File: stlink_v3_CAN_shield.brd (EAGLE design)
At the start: 64.8 x 40.6 mm, 13 parts, among them CON1 STLINK_V3, U1 MCP2562-E/SN

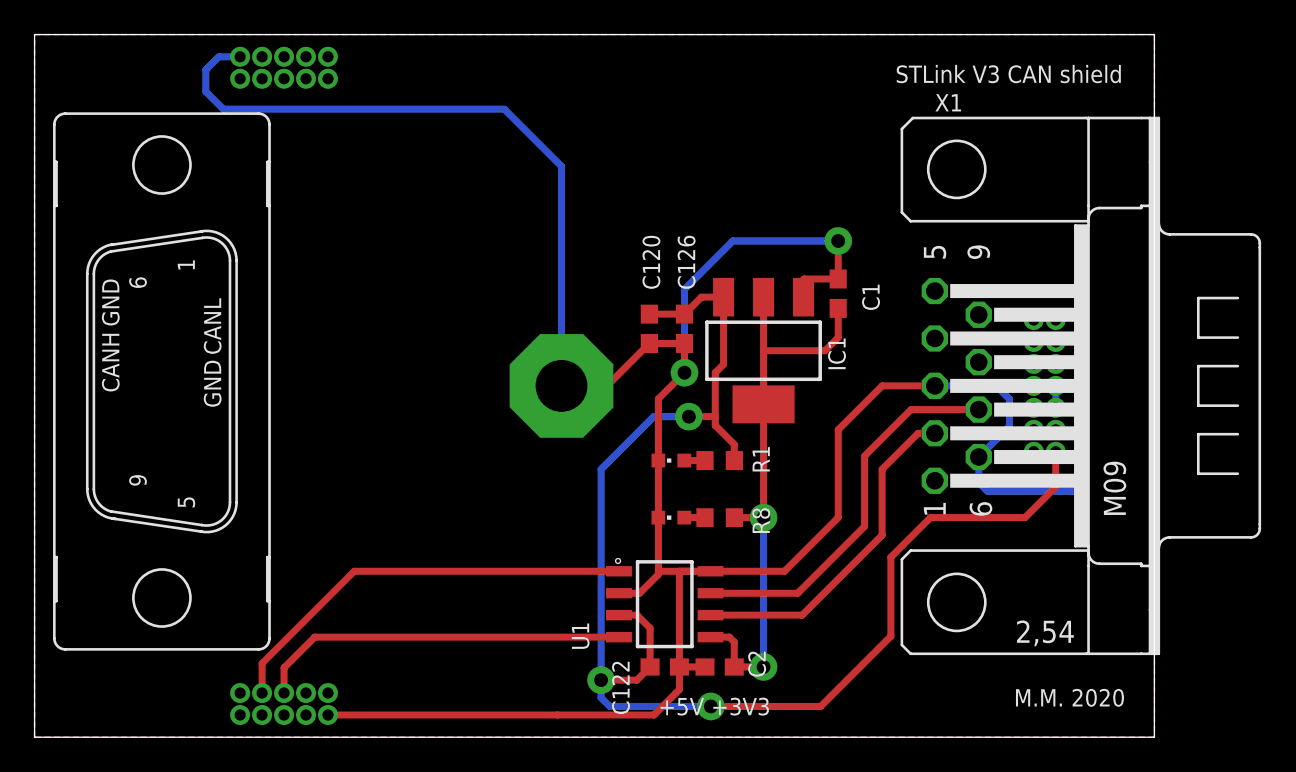
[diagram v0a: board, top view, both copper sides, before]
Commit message: Update STLink footprint
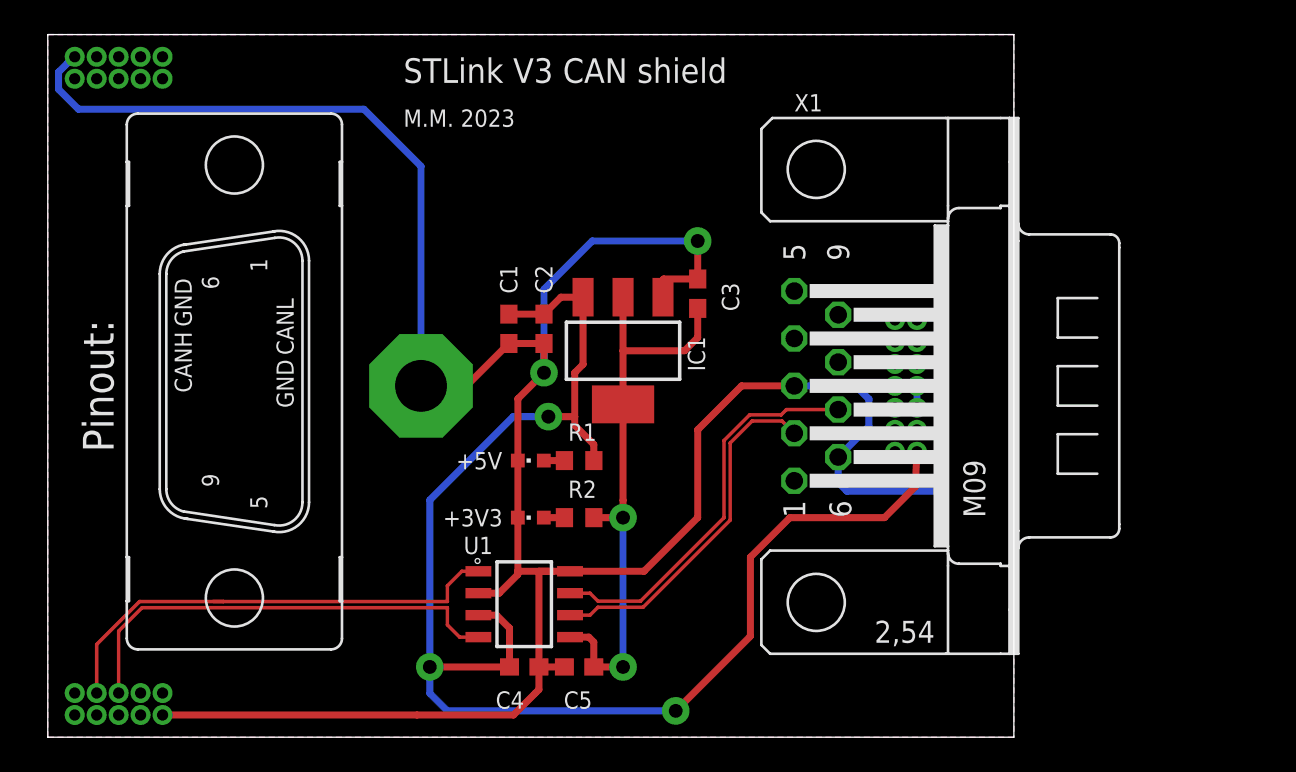
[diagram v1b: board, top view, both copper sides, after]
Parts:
- removed C120: 1uF, rcl:C0603
- removed C122: 100n, rcl:C0603
- removed C126: 10n, rcl:C0603
- removed R8: 330, rcl:R0603
- added C3, C4: 100n, rcl:C0603
- added C5: 1uF, rcl:C0603
- added R2: 330, rcl:R0603
- C1: value 100n -> 1uF
- C2: value 1uF -> 10n
- moved C2 22.0 mm to (28.7, 23.6), turned to 270 degrees
- moved C1 19.2 mm to (26.7, 23.6)
- moved LED1 8.77 mm to (27.9, 16.0)
- moved LED2 8.77 mm to (27.9, 12.7)
- moved CON1 8.13 mm to (21.6, 20.3)
- moved IC1 8.13 mm to (33.3, 22.4)
- moved R1 8.13 mm to (30.7, 16.0)
- moved X1 8.13 mm to (44.5, 20.3)
- moved U1 8.13 mm to (27.6, 7.69)
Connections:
- net CAN_H renamed CAN_P
- net CAN_L renamed CAN_N
- net CAN_RX renamed CAN_MCU_N
- net CAN_TX renamed CAN_MCU_P
- net +3V3: now also C3.2, C5.1, R2.1; no longer C1.2, C2.1, R8.1
- net GND: now also C1.2, C3.1, C4.1, C5.2; no longer C1.1, C120.2, C122.1, C126.2
- net VIN_LED_R1: now also LED2.A, R2.2; no longer LED1.A, R8.2
- net VIN_LED_R2: now also LED1.A; no longer LED2.A
- net VUSB: now also C1.1, C2.1, C4.2; no longer C120.1, C122.2, C126.1
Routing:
- net CAN_MCU_N: track 21.6 -> 26.2 mm
- net VUSB: track 79.9 -> 83.9 mm
- net CAN_MCU_P: track 24.6 -> 27.8 mm
- net CAN_N: track 19.6 -> 20.5 mm
- net CAN_P: track 22.3 -> 22.9 mm
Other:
- board size 64.8 x 40.6 mm -> 55.9 x 40.6 mm
- board text added: "+3V3"
- board text added: "+5V"
- board text added: "M.M. 2023"
- board text added: "Pinout:"
- board text removed: "+5V +3V3"
- board text removed: ">VALUE"
- board text removed: "M.M. 2020"
